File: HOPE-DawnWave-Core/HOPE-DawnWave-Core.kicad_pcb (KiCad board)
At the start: 2 copper layers, 44.6 x 48 mm, 50 parts, among them J1 USB_C_Receptacle_USB2.0_16P, J2 Screw_Terminal_01x02, SW1 RST, SW2 BOOT, U1 TLV62569DRL, U2 USBLC6-2P6, U3 ESP32-C6-WROOM-1, U4 MAX98357A, U5 BME688, X1 EYE_SPI_DISPLAY_FLIP

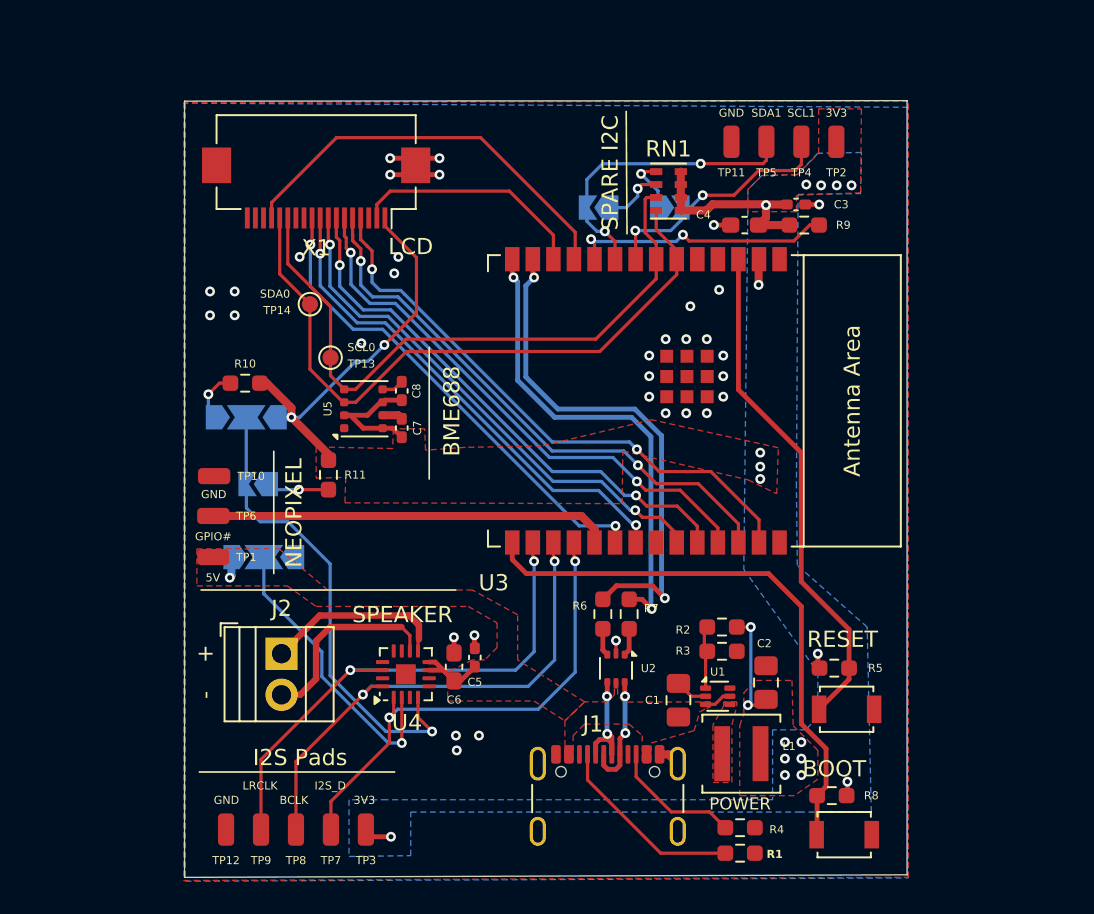
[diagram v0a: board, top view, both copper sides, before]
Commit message: fixed spacing on high speed lines, added ground via stitching, made power polygons a bit cleaner, silkscreen labeling is still not done but all warnings are gone
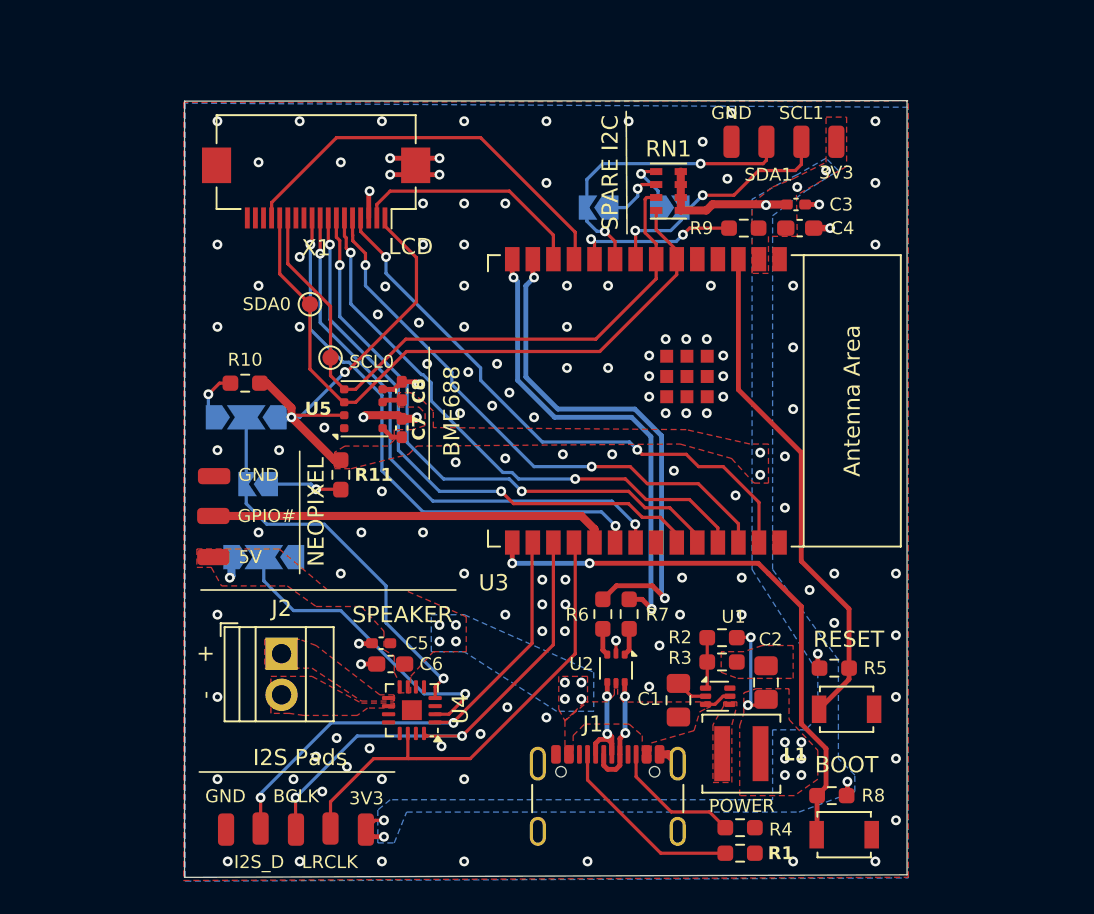
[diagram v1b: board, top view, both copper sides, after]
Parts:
- moved C5 5.86 mm to (137.1, 103.4), turned to 180 degrees
- moved TP7 4.34 mm to (129.7, 114.8)
- moved TP9 4.29 mm to (134.0, 114.8)
- moved C6 3.92 mm to (137.7, 104.6), turned to 180 degrees
- moved R9 3.74 mm to (159.5, 77.7), turned to 180 degrees
- moved C4 3.41 mm to (163.0, 77.7), turned to 0 degrees
- moved U4 2.25 mm to (139.0, 107.5), turned to 180 degrees
- moved R11 0.76 mm to (134.6, 93.0)
- moved R2 0.66 mm to (158.2, 103.0)
- moved R3 0.66 mm to (158.2, 104.5)
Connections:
- U3 pad 16: MCU_LRCLK -> MCU_I2S_D
- U3 pad 18: MCU_I2S_D -> MCU_LRCLK
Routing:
- net /MAX98357A_I2S/Speaker_N: track 12.2 -> 0.00 mm
- net /MAX98357A_I2S/Speaker_P: track 11.3 -> 0.00 mm
- net +3.3V: track 57.4 -> 50.8 mm, vias 22 -> 19
- net Net-(U3-GPIO8): track 16.2 -> 10.2 mm
- net VBUS: track 8.50 -> 3.02 mm, vias 1 -> 9
- net GND: track 17.4 -> 22.4 mm, vias 34 -> 131
- net Net-(JP3-C): track 29.3 -> 24.8 mm
- net MCU_SD_SEL: track 30.3 -> 34.6 mm
- net MCU_LRCLK: track 32.7 -> 29.0 mm, vias 2 -> 0
- net MCU_DISP_SEL: track 31.0 -> 34.6 mm
- net MCU_DRST: track 32.6 -> 36.0 mm
- net MCU_D/C: track 33.5 -> 36.4 mm
- net MCU_MISO: track 34.1 -> 35.4 mm
- net Net-(JP4-C): track 18.3 -> 19.3 mm
- net MCU_BCLK: track 31.5 -> 30.5 mm
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- added copper zone on F.Cu, net /MAX98357A_I2S/Speaker_N
- added copper zone on F.Cu, net /MAX98357A_I2S/Speaker_P
- added copper zone on B.Cu, net VBUS

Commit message: corrected eyespi connector wiring and added a 2.54mm pitch header to break it out in case something bad happens
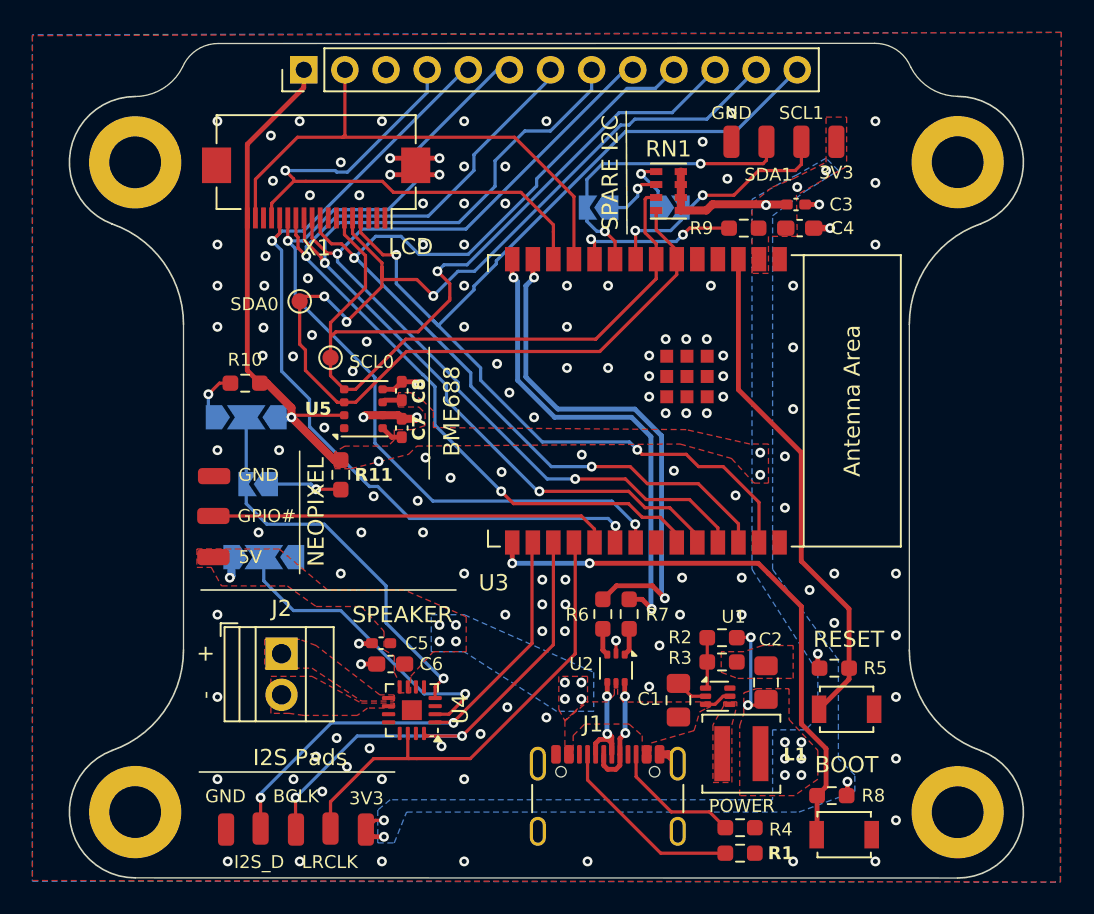
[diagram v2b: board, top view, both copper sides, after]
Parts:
- added H1: MountingHole, MountingHole:MountingHole_3.2mm_M3_ISO7380_Pad, F.Cu at (121.9, 113.8)
- added H2: MountingHole, MountingHole:MountingHole_3.2mm_M3_ISO7380_Pad, F.Cu at (121.9, 73.7)
- added H3: MountingHole, MountingHole:MountingHole_3.2mm_M3_ISO7380_Pad, F.Cu at (172.7, 73.6)
- added H4: MountingHole, MountingHole:MountingHole_3.2mm_M3_ISO7380_Pad, F.Cu at (172.7, 113.8)
- added J3: Conn_01x13_Pin, Connector_PinHeader_2.54mm:PinHeader_1x13_P2.54mm_Vertical, F.Cu at (132.3, 67.9)
- moved TP14 0.66 mm to (132.1, 82.2)
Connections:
- U3 pad 11: MCU_TD -> MCU_BACKLIGHT
- U3 pad 12: MCU_BACKLIGHT -> MCU_SCLK
- U3 pad 20: MCU_SD_SEL -> MCU_MOSI
- U3 pad 21: MCU_DISP_SEL -> MCU_MISO
- U3 pad 23: MCU_DRST -> MCU_D/C
- U3 pad 24: MCU_D/C -> MCU_DRST
- U3 pad 25: MCU_MISO -> MCU_DISP_SEL
- U3 pad 26: MCU_MOSI -> MCU_SD_SEL
- U3 pad 27: MCU_SCLK -> MCU_TD
- X1 pad 1: +3.3V -> /2.8" TFT display through EYESPI/GPIO2
- X1 pad 10: MCU_SD_SEL -> MCU_DISP_SEL
- X1 pad 11: /2.8" TFT display through EYESPI/MEM_CS -> MCU_DRST
- X1 pad 12: /2.8" TFT display through EYESPI/TSCS -> MCU_D/C
- X1 pad 13: MCU_SCL0 -> MCU_MISO
- X1 pad 14: MCU_SDA0 -> MCU_MOSI
- X1 pad 15: MCU_TD -> MCU_SCLK
- X1 pad 16: /2.8" TFT display through EYESPI/BUSY -> GND
- X1 pad 17: /2.8" TFT display through EYESPI/GPIO1 -> MCU_BACKLIGHT
- X1 pad 18: /2.8" TFT display through EYESPI/GPIO2 -> +3.3V
- X1 pad 2: MCU_BACKLIGHT -> /2.8" TFT display through EYESPI/GPIO1
- X1 pad 3: GND -> /2.8" TFT display through EYESPI/BUSY
- X1 pad 4: MCU_SCLK -> MCU_TD
- X1 pad 5: MCU_MOSI -> MCU_SDA0
- X1 pad 6: MCU_MISO -> MCU_SCL0
- X1 pad 7: MCU_D/C -> /2.8" TFT display through EYESPI/TSCS
- X1 pad 8: MCU_DRST -> /2.8" TFT display through EYESPI/MEM_CS
- X1 pad 9: MCU_DISP_SEL -> MCU_SD_SEL
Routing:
- net MCU_TD: track 25.5 -> 66.0 mm, vias 0 -> 2
- net MCU_SDA0: track 41.4 -> 77.9 mm, vias 0 -> 3
- net MCU_SCL0: track 40.1 -> 73.1 mm, vias 0 -> 1
- net MCU_SD_SEL: track 34.6 -> 61.6 mm
- net MCU_DISP_SEL: track 34.6 -> 58.1 mm
- net MCU_DRST: track 36.0 -> 58.3 mm
- net MCU_D/C: track 36.4 -> 55.7 mm
- net MCU_MISO: track 35.4 -> 54.6 mm
- net MCU_BACKLIGHT: track 14.7 -> 32.9 mm
- net MCU_MOSI: track 35.2 -> 53.0 mm
- net +3.3V: track 50.8 -> 55.3 mm, vias 19 -> 18
- net GND: track 22.4 -> 20.7 mm, vias 131 -> 135
- net MCU_SCLK: track 35.9 -> 35.2 mm, vias 2 -> 1
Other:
- board size 44.6 x 48 mm -> 58.9 x 51.6 mm

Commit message: a bit better
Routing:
- net GND: vias 135 -> 139
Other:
- board text added: "GPIO21"
- board text removed: "GPIO#"
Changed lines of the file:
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@@
 	)
 	(gr_line
-		(start 132.08 99.0626)
-		(end 132.08 91.5061)
+		(start 133.7564 99.02825)
+		(end 133.7564 91.47175)
 		(stroke
 			(width 0.1)
@@
 		)
 	)
-	(gr_text "GPIO#"
+	(gr_text "GPIO21"
 		(at 130.048 95.504 0)
 		(layer "F.SilkS")
@@
 	)
 	(gr_text "NEOPIXEL"
-		(at 133.096 95.25 90)
+		(at 132.9436 95.25 90)
 		(layer "F.SilkS")
 		(effects
@@
 	)
 	(via
+		(at 130.175 67.945)
+		(size 0.6096)
+		(drill 0.3048)
+		(layers "F.Cu" "B.Cu")
+		(free yes)
+		(net 3)
+	)
+	(via
 		(at 144.78 101.6)
 		(size 0.6096)
@@
 	)
 	(via
+		(at 167.64 67.945)
+		(size 0.6096)
+		(drill 0.3048)
+		(layers "F.Cu" "B.Cu")
+		(free yes)
+		(net 3)
+	)
+	(via
 		(at 164.846 77.724)
 		(size 0.6096)
@@
 	)
 	(via
+		(at 165.1 67.945)
+		(size 0.6096)
+		(drill 0.3048)
+		(layers "F.Cu" "B.Cu")
+		(free yes)
+		(net 3)
+	)
+	(via
 		(at 144.78 73.914)
 		(size 0.6096)
@@
 		(size 0.6096)
 		(drill 0.3048)
+		(layers "F.Cu" "B.Cu")
+		(free yes)
+		(net 3)
+	)
+	(via
+		(at 127 67.945)
+		(size 0.6096)
+		(drill 0.3048)

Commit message: functional silkscreen complete
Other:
- board text added: "Bridge for L+R"
- board text added: "Gain: 12-9-6 dB"
- board text added: "Mono: L R"
- board text removed: "GAIN SELECT"
- board text removed: "LR SELECT"
- board text removed: "MONO SELECT"
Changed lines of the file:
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@@
 		(layer "Edge.Cuts")
 	)
-	(gr_text "LR SELECT"
-		(at 129.032 87.376 0)
+	(gr_text "Mono: L    R"
+		(at 130.7592 87.376 0)
 		(layer "B.SilkS")
 		(effects
@@
 		)
 	)
-	(gr_text "MONO SELECT"
-		(at 129.47 91.567 0)
+	(gr_text "Bridge for L+R"
+		(at 136.2456 93.472 0)
 		(layer "B.SilkS")
 		(effects
@@
 		)
 	)
-	(gr_text "GAIN SELECT"
-		(at 129.946 96.0768 0)
+	(gr_text "Gain: 12-9-6 dB"
+		(at 130.9624 96.1644 0)
 		(layer "B.SilkS")
 		(effects

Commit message: fab files generated, pcb finalized
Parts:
- removed JP4: GAIN_SEL, Jumper:SolderJumper-3_P2.0mm_Open_TrianglePad1.0x1.5mm
- added R12: 0R, Resistor_SMD:R_0402_1005Metric_Pad0.72x0.64mm_HandSolder, B.Cu at (128.2, 98.4)
- added R13: 0R, Resistor_SMD:R_0402_1005Metric_Pad0.72x0.64mm_HandSolder, B.Cu at (130.8, 98.4)
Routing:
- net MCU_SDA0: track 77.9 -> 64.5 mm
- net MCU_SCL0: track 73.1 -> 61.5 mm
- net /MCU_USB_D-: track 32.0 -> 26.8 mm
- net /MCU_USB_D+: track 29.6 -> 25.1 mm
- net VBUS: track 3.02 -> 5.56 mm
- net Net-(U4-GAIN_SLOT): track 19.3 -> 20.3 mm
- net GND: vias 139 -> 138
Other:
- board text added: "Gain (dB): 12-9-6"
- board text removed: "Gain: 12-9-6 dB"

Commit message: whoa thats a lot of manufacturing files
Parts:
- moved X1 1.15 mm to (134.2, 75.2)
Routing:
- net GND: track 20.7 -> 23.5 mm, vias 138 -> 139
- net MCU_TD: track 66.0 -> 65.2 mm
- net +3.3V: track 55.3 -> 54.4 mm
- net MCU_SD_SEL: track 61.6 -> 60.9 mm
- net MCU_DISP_SEL: track 58.1 -> 57.4 mm
- net MCU_BACKLIGHT: track 32.9 -> 32.1 mm
- net MCU_SCLK: track 35.2 -> 34.7 mm
